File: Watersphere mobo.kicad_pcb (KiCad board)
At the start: 2 copper layers, 74.9 x 81.3 mm, 80 parts, among them IC1 BQ25303JRTER, J2 Conn_01x01_Pin, J3 Conn_01x01_Pin, J4 691213710002, J5 Pressure Sensor I/O, U1 ADS1115IDGSR, U12 LP55231SQE_NOPB, U2 ADS1115IDGSR, U3 TPS63001DRCR, U4 BNO055, U5 ADP1109AN-12, U6 ADP1109AN-12, U7 ADA3708, U8 MIC2876-5.0YMT-TR

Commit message: Routing begin
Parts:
- removed D2, D3: 1N5818, Diode_THT:D_DO-41_SOD81_P10.16mm_Horizontal
- added C16: 1 uF, Capacitor_SMD:C_0603_1608Metric_Pad1.08x0.95mm_HandSolder, F.Cu at (68.1, 78.1)
- added C30: 22uF, Capacitor_SMD:C_0603_1608Metric_Pad1.08x0.95mm_HandSolder, F.Cu at (51.4, 43.4)
- added C31: 22uF, Capacitor_SMD:C_0603_1608Metric_Pad1.08x0.95mm_HandSolder, F.Cu at (53.9, 43.4)
- added C32: 22uF, Capacitor_SMD:C_0603_1608Metric_Pad1.08x0.95mm_HandSolder, F.Cu at (56.4, 43.4)
- added C33: 2.2uF, Capacitor_SMD:C_0603_1608Metric_Pad1.08x0.95mm_HandSolder, F.Cu at (59.8, 39.9)
- added C34: 4.7nf, Capacitor_SMD:C_0603_1608Metric_Pad1.08x0.95mm_HandSolder, F.Cu at (53.2, 38.2)
- added C35: optional, Capacitor_SMD:C_0603_1608Metric_Pad1.08x0.95mm_HandSolder, F.Cu at (54.0, 40.8)
- added C36: optional, Capacitor_SMD:C_0603_1608Metric_Pad1.08x0.95mm_HandSolder, F.Cu at (50.2, 52.3)
- added C37: 4.7nf, Capacitor_SMD:C_0603_1608Metric_Pad1.08x0.95mm_HandSolder, F.Cu at (51.9, 52.3)
- added C38: 22uF, Capacitor_SMD:C_0603_1608Metric_Pad1.08x0.95mm_HandSolder, F.Cu at (61.7, 51.4)
- added C39: 22uF, Capacitor_SMD:C_0603_1608Metric_Pad1.08x0.95mm_HandSolder, F.Cu at (53.5, 56.0)
- added C40: 100nF, Capacitor_SMD:C_0603_1608Metric_Pad1.08x0.95mm_HandSolder, F.Cu at (60.8, 58.3)
- added C41: 22uF, Capacitor_SMD:C_0603_1608Metric_Pad1.08x0.95mm_HandSolder, F.Cu at (51.2, 56.0)
- added C42: 22uF, Capacitor_SMD:C_0603_1608Metric_Pad1.08x0.95mm_HandSolder, F.Cu at (55.7, 56.0)
- added C43: 2.2uF, Capacitor_SMD:C_0603_1608Metric_Pad1.08x0.95mm_HandSolder, F.Cu at (59.1, 52.8)
- added J6: Pressure Sensor I/O, Connector_PinHeader_2.54mm:PinHeader_1x03_P2.54mm_Vertical, F.Cu at (69.7, 96.9)
- added J7: Pressure Sensor I/O, Connector_PinHeader_2.54mm:PinHeader_1x03_P2.54mm_Vertical, F.Cu at (58.3, 96.9)
- added R19: 301k, Resistor_SMD:R_0603_1608Metric_Pad0.98x0.95mm_HandSolder, F.Cu at (61.5, 41.5)
- added R20: 681k, Resistor_SMD:R_0603_1608Metric_Pad0.98x0.95mm_HandSolder, F.Cu at (58.2, 39.9)
- added R21: 107k, Resistor_SMD:R_0603_1608Metric_Pad0.98x0.95mm_HandSolder, F.Cu at (56.5, 39.9)
- added R22: 127k, Resistor_SMD:R_0603_1608Metric_Pad0.98x0.95mm_HandSolder, F.Cu at (57.5, 46.5)
- added R23: 17.4k, Resistor_SMD:R_0603_1608Metric_Pad0.98x0.95mm_HandSolder, F.Cu at (54.9, 38.2)
- added R24: 17.4k, Resistor_SMD:R_0603_1608Metric_Pad0.98x0.95mm_HandSolder, F.Cu at (53.7, 52.3)
- added R25: 681k, Resistor_SMD:R_0603_1608Metric_Pad0.98x0.95mm_HandSolder, F.Cu at (56.4, 53.1)
- added R26: 127k, Resistor_SMD:R_0603_1608Metric_Pad0.98x0.95mm_HandSolder, F.Cu at (56.9, 59.3)
- added R27: 107k, Resistor_SMD:R_0603_1608Metric_Pad0.98x0.95mm_HandSolder, F.Cu at (56.4, 51.3)
- added R28: 301k, Resistor_SMD:R_0603_1608Metric_Pad0.98x0.95mm_HandSolder, F.Cu at (60.8, 54.7)
- C14: value 10 uF -> 22uF
- C15: value 10 uF -> 100nF
- J5: footprint Connector_PinSocket_2.54mm:PinSocket_1x03_P2.54mm_Horizontal -> Connector_PinHeader_2.54mm:PinHeader_1x03_P2.54mm_Vertical
- L3, L4: value L -> 1.8uH; footprint 12v Power Ind:46473C -> 9V_Power_IND:IND_7030-WE-LHMI_WRE-L
- Pump1Controller1, Pump2Controller1, ReactionWheel1Controller1, ReactionWheel2Controller1: footprint Motor_Controller:SOT6_DRV8212_TEX -> DRV8212:SOT6_DRV8212_TEX-L
- U5, U6: value ADP1109AN-12 -> TPS61089RNRR; footprint ADP1109:N_8_ADI -> TPS61089:IC_TPS61089RNRR
- moved R18 112.7 mm to (59.2, 84.7), turned to 90 degrees
- moved C11 110.4 mm to (51.6, 72.3)
- moved C27 107.3 mm to (56.3, 83.7), turned to 180 degrees
- moved C28 107.2 mm to (56.3, 85.6), turned to 180 degrees
- moved R9 102.1 mm to (63.8, 68.3), turned to -90 degrees
- moved R8 102.0 mm to (63.8, 64.8), turned to -90 degrees
- moved R15 100.9 mm to (69.6, 68.3), turned to -90 degrees
- moved C29 100.6 mm to (61.7, 81.5), turned to -90 degrees
- moved R11 99.7 mm to (65.8, 68.3), turned to -90 degrees
- moved R10 99.7 mm to (65.8, 64.8), turned to -90 degrees
- moved R6 99.3 mm to (61.7, 64.8), turned to -90 degrees
- moved R7 99.3 mm to (61.7, 68.3), turned to -90 degrees
- moved R13 97.7 mm to (67.7, 64.8), turned to 90 degrees
- moved R12 97.7 mm to (67.7, 68.3), turned to 90 degrees
- moved R14 95.9 mm to (69.6, 64.8), turned to -90 degrees
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- renumbered RW1 to ReactionWheel1, RW2 to ReactionWheel2
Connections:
- net 12v(1)_meas renamed 9v(1)_meas
- net 12v(2)_meas renamed 9v(2)_meas
- 100uF1 pad 1: 12v(1) -> 9v(1)
- 100uF2 pad 1: 12v(2) -> 9v(2)
- 100uF3 pad 1: 12v(1) -> 9v(1)
- 100uF4 pad 1: 12v(2) -> 9v(2)
- C12 pad 1: 12v(1) -> 9v(1)
- C13 pad 1: 12v(2) -> 9v(2)
- C14 pad 1: 12v(1) -> BAT+
- C15 pad 1: 12v(2) -> Net-(U5-BOOT)
- C15 pad 2: GND -> Net-(U5-SW)
- C21 pad 1: 12v(1) -> 9v(1)
- C22 pad 1: 12v(2) -> 9v(2)
- D1 pad 1: (no net) -> Net-(D1-PadA)
- D1 pad 2: (no net) -> Net-(IC1-STAT)
- L3 pad 1: Net-(D2-A) -> BAT+
- L3 pad 2: BAT+ -> Net-(U5-SW)
- L4 pad 1: Net-(D3-A) -> BAT+
- L4 pad 2: BAT+ -> Net-(U6-SW)
- Pump1Controller1 pad 5: 12v(1) -> 9v(1)
- Pump2Controller1 pad 5: 12v(2) -> 9v(2)
- R12 pad 1: 12v(1)_Shutdown -> 9v(1)
- R14 pad 1: 12v(2)_Shutdown -> 9v(2)
- R18 pad 2: BNO_BOOTN -> Net-(U4-NBOOT_LOAD_PIN)
- ReactionWheel1Controller1 pad 5: 12v(1) -> 9v(1)
- ReactionWheel2Controller1 pad 5: 12v(2) -> 9v(2)
- U4 pad 11: unconnected-(U4-NRESET-Pad11) -> BNO_BOOTN
- U4 pad 17: unconnected-(U4-COM3-Pad17) -> GND
- U4 pad 4: BNO_BOOTN -> Net-(U4-NBOOT_LOAD_PIN)
- U4 pad 5: unconnected-(U4-PS1-Pad5) -> GND
- U4 pad 6: unconnected-(U4-PS0-Pad6) -> GND
- U5 pad 1: BAT+ -> Net-(U5-FSW)
- U5 pad 2: unconnected-(U5-NC-Pad2) -> Net-(U5-VCC)
- U5 pad 3: Net-(D2-A) -> Net-(U5-FB)
- U5 pad 4: GND -> Net-(U5-COMP)
- U5 pad 5: unconnected-(U5-NC-Pad5) -> GND
- U5 pad 6: unconnected-(U5-NC-Pad6) -> 9v(1)
- U5 pad 7: 12v(1)_Shutdown -> 9v(1)_Shutdown
- U5 pad 8: 12v(1) -> Net-(U5-ILIM)
- U6 pad 1: BAT+ -> Net-(U6-FSW)
- U6 pad 2: unconnected-(U6-NC-Pad2) -> Net-(U6-VCC)
- U6 pad 3: Net-(D3-A) -> Net-(U6-FB)
- U6 pad 4: GND -> Net-(U6-COMP)
- U6 pad 5: unconnected-(U6-NC-Pad5) -> GND
- U6 pad 6: unconnected-(U6-NC-Pad6) -> 9v(2)
- U6 pad 7: 12v(2)_Shutdown -> 9v(2)_Shutdown
- U6 pad 8: 12v(2) -> Net-(U6-ILIM)
- U7 pad 4: +5v -> Rasp_Vsupply
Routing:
- net BAT+: track 0.00 -> 112.2 mm
- net REGN: track 0.00 -> 12.9 mm, vias 0 -> 2
- net Net-(U3-EN): track 0.00 -> 11.8 mm
- net VIN: track 0.00 -> 11.3 mm
- net +3.3V: track 0.00 -> 7.66 mm
- net Net-(IC1-ICHG): track 0.00 -> 7.33 mm
- net Net-(U3-L1): track 0.00 -> 5.42 mm
- net Net-(U3-L2): track 0.00 -> 5.23 mm
- net Net-(IC1-TS): track 0.00 -> 5.19 mm
- net Net-(IC1-STAT): track 0.00 -> 4.77 mm
- net Net-(IC1-SW_1): track 0.00 -> 4.40 mm
- net Net-(IC1-BTST): track 0.00 -> 4.24 mm
- net Net-(J1-VCC): track 0.00 -> 2.80 mm
- net Net-(D1-PadA): track 0.00 -> 2.27 mm
- net Net-(IC1-PMID): track 0.00 -> 2.21 mm
- added copper zone on F.Cu, net GND
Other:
- outline, holes or cut-outs redrawn
- copper layers 2 -> 4
- board text added: "P2"
- board text added: "RW1"
- board text added: "RW2"
- board text removed: "D3"

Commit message: Deesign Rules
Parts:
- U5: value TPS61089RNRR -> |
- moved R16 25.1 mm to (51.0, 77.3), turned to -90 degrees
- moved R17 25.0 mm to (48.5, 77.4), turned to -90 degrees
- moved C23 4.74 mm to (42.6, 22.4), turned to 0 degrees
- moved U12 4.54 mm to (37.4, 20.5)
- moved R13 3.58 mm to (67.7, 68.3), turned to -90 degrees
- moved R12 3.53 mm to (67.7, 64.8), turned to -90 degrees
- moved C24 2.58 mm to (48.8, 25.9), turned to 0 degrees
- moved C25 2.24 mm to (43.8, 20.0)
- moved C26 1.99 mm to (48.8, 27.5)
- moved C11 1.24 mm to (52.6, 71.6)
- moved C27 1.22 mm to (56.4, 84.9)
- moved C28 1.22 mm to (56.3, 86.8)
- moved R18 1.22 mm to (59.2, 85.9)
- moved C20 0.98 mm to (81.9, 66.5)
- moved C29 0.55 mm to (61.2, 81.5)
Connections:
- D1 pad 1: Net-(D1-PadA) -> (no net)
- D1 pad 2: Net-(IC1-STAT) -> (no net)
- U12 pad 25: (no net) -> GND
- U2 pad 6: unconnected-(U2-AIN2-Pad6) -> Misc. Sensor 1
- U2 pad 7: unconnected-(U2-AIN3-Pad7) -> Misc. Sensor 2
- U3 pad 12: (no net) -> GND
- U3 pad 13: (no net) -> GND
- U3 pad 14: (no net) -> GND
- U3 pad 15: (no net) -> GND
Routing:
- net +5v: track 0.00 -> 170.6 mm, vias 0 -> 6
- net I2C_Bus1_SDA: track 0.00 -> 141.1 mm, vias 0 -> 4
- net I2C_Bus1_SCL: track 0.00 -> 140.5 mm, vias 0 -> 5
- net 9v(2): track 0.00 -> 109.6 mm, vias 0 -> 4
- net +3.3V: track 7.66 -> 116.7 mm, vias 0 -> 4
- net 9v(1): track 0.00 -> 105.1 mm, vias 0 -> 5
- net PWM_4: track 0.00 -> 63.8 mm, vias 0 -> 2
- net PWM_3: track 0.00 -> 58.2 mm, vias 0 -> 2
- net GND: track 0.00 -> 53.2 mm, vias 0 -> 29
- net BNO_BOOTN: track 0.00 -> 51.6 mm, vias 0 -> 1
- net PWM_2: track 0.00 -> 47.9 mm, vias 0 -> 2
- net BNO_Data_Ready: track 0.00 -> 47.4 mm, vias 0 -> 1
- net PWM_1: track 0.00 -> 44.2 mm, vias 0 -> 2
- net Misc. Sensor 2: track 0.00 -> 43.9 mm, vias 0 -> 1
- net BAT+: track 112.2 -> 155.8 mm
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- added copper zone on B.Cu, net GND
- added copper zone on In1.Cu, net GND
- added copper zone on In2.Cu, net GND

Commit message: gps started
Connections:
- D1 pad 1: (no net) -> Net-(D1-PadA)
- D1 pad 2: (no net) -> Net-(IC1-STAT)
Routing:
- net GND: track 53.2 -> 103.5 mm, vias 29 -> 34
- net +5v: track 170.6 -> 151.6 mm
- net +3.3V: track 116.7 -> 128.9 mm, vias 4 -> 5
- net I2C_Bus1_SDA: track 141.1 -> 147.1 mm

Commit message: Tedi Check dis over pls.
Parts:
- added C17: 10 uF, Capacitor_SMD:C_0603_1608Metric_Pad1.08x0.95mm_HandSolder, F.Cu at (66.7, 82.2)
- added C18: 100nF, Capacitor_SMD:C_0603_1608Metric_Pad1.08x0.95mm_HandSolder, F.Cu at (66.7, 79.7)
- added J8: JST_02, Connector_JST:JST_EH_B2B-EH-A_1x02_P2.50mm_Vertical, F.Cu at (34.3, 96.3)
- added Q1: AO3400A, N-Channel:SOT95P280X125-3N, F.Cu at (29.0, 93.3)
- added R29: 10k, Resistor_SMD:R_0603_1608Metric_Pad0.98x0.95mm_HandSolder, F.Cu at (24.0, 93.6)
- added U10: 734120114, UFL:73412-0114_MOL, F.Cu at (88.2, 80.4)
- added U9: TESEO-LIV3R, Teseo Liv3r:ARRAY_LIV3R_STM, F.Cu at (74.0, 77.2)
- U5: value | -> TPS61089RNRR
- moved C16 3.45 mm to (64.6, 77.7)
- moved MC1 3.45 mm to (63.5, 74.4)
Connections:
- U7 pad 29: unconnected-(U7-GPIO5-Pad29) -> Solenoid_Driver
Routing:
- net Solenoid_Driver: track 0.00 -> 64.9 mm
- net I2C_Bus1_SDA: track 147.1 -> 160.3 mm, vias 4 -> 6
- net I2C_Bus1_SCL: track 140.5 -> 148.9 mm, vias 5 -> 7
- net Net-(U10-SIGNAL): track 0.00 -> 8.01 mm
- net GND: track 103.5 -> 97.7 mm, vias 34 -> 42
- net +3.3V: track 128.9 -> 134.4 mm
- net Net-(J8-Pad1): track 0.00 -> 5.11 mm
- net +5v: track 151.6 -> 152.7 mm
- net 9v(1): vias 5 -> 4
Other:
- outline, holes or cut-outs redrawn

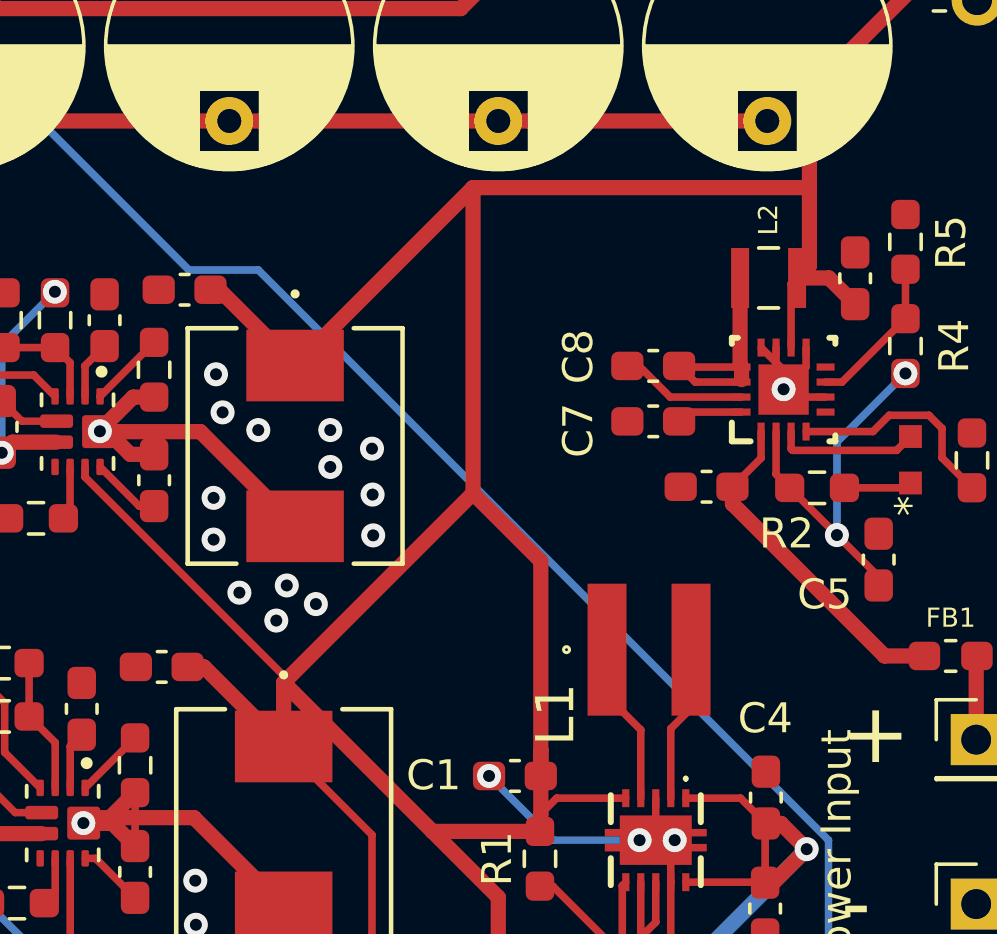
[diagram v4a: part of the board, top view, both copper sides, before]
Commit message: Updated a couple traces
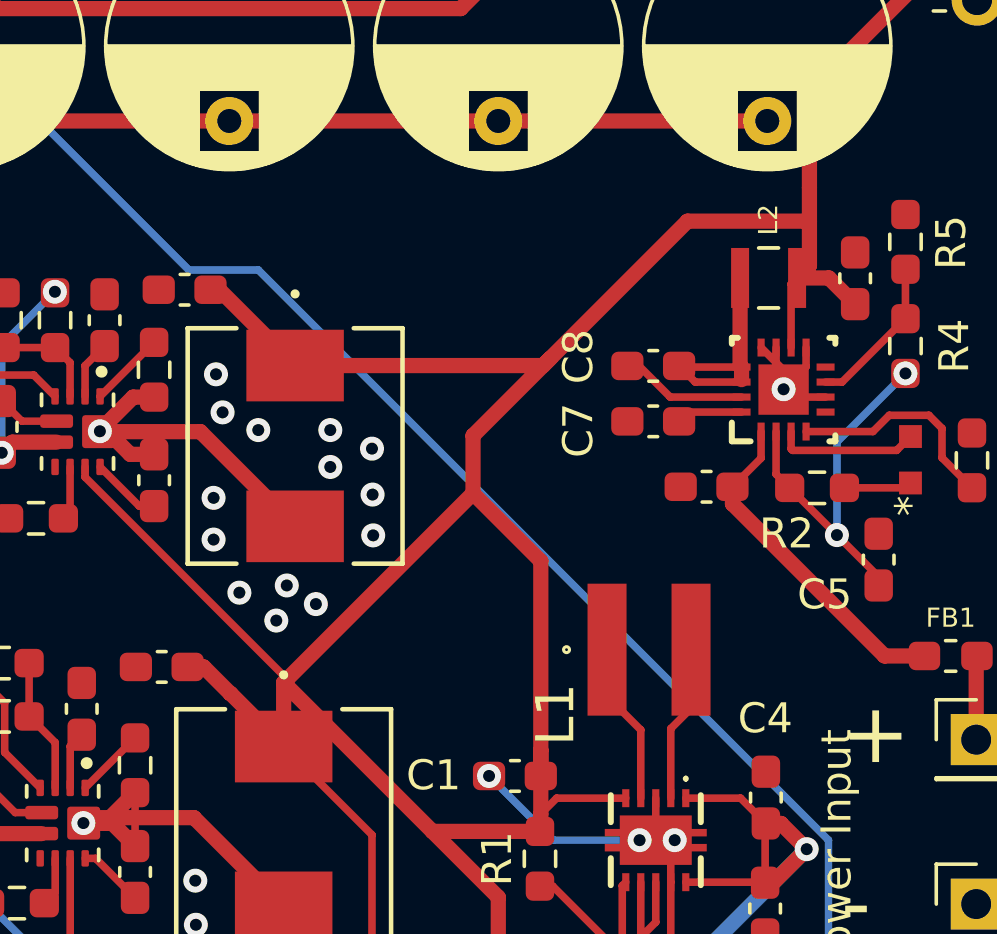
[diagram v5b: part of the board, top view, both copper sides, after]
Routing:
- net BAT+: track 155.8 -> 150.7 mm
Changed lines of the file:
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@@
   (segment (start 74.3575 56.3372) (end 74.3575 56.89) (width 0.508) (layer "F.Cu") (net 1))
   (segment (start 61.722 63.8735) (end 58.67 60.8215) (width 0.254) (layer "F.Cu") (net 1))
+  (segment (start 64.008 52.324) (end 63.119 51.435) (width 0.508) (layer "F.Cu") (net 1))
   (segment (start 58.67 60.8215) (end 58.67 57.817) (width 0.254) (layer "F.Cu") (net 1))
+  (segment (start 83.312 35.4584) (end 83.312 36.576) (width 0.508) (layer "F.Cu") (net 1))
   (segment (start 74.9703 68.663) (end 75.5678 69.2605) (width 0.254) (layer "F.Cu") (net 1))
+  (segment (start 72.0979 45.64741) (end 72.0979 43.7261) (width 0.508) (layer "F.Cu") (net 1))
   (segment (start 74.2703 67.5805) (end 74.9703 67.5805) (width 0.508) (layer "F.Cu") (net 1))
   (segment (start 61.722 63.8735) (end 63.4455 62.15) (width 0.254) (layer "F.Cu") (net 1))
-  (segment (start 83.312 35.4584) (end 83.312 38.057997) (width 0.508) (layer "F.Cu") (net 1))
-  (segment (start 72.0979 35.4584) (end 66.167 41.3893) (width 0.508) (layer "F.Cu") (net 1))
   (segment (start 82.7 38.669997) (end 82.9 38.469997) (width 0.254) (layer "F.Cu") (net 1))
   (segment (start 63.4455 62.15) (end 67.16 62.15) (width 0.254) (layer "F.Cu") (net 1))
@@
   (segment (start 78.24 68.25) (end 79.107 69.117) (width 0.254) (layer "F.Cu") (net 1))
   (segment (start 65.786 51.728324) (end 65.786 54.0893) (width 0.254) (layer "F.Cu") (net 1))
+  (segment (start 63.119 51.435) (end 62.5845 51.435) (width 0.508) (layer "F.Cu") (net 1))
   (segment (start 72.0979 45.64741) (end 74.3575 47.90701) (width 0.508) (layer "F.Cu") (net 1))
   (segment (start 76.5783 68.25) (end 78.24 68.25) (width 0.254) (layer "F.Cu") (net 1))
@@
   (segment (start 77.19 55.81) (end 74.8847 55.81) (width 0.254) (layer "F.Cu") (net 1))
   (segment (start 65.786 51.95931) (end 70.74419 56.9175) (width 0.508) (layer "F.Cu") (net 1))
+  (segment (start 83.312 36.576) (end 83.312 38.057997) (width 0.508) (layer "F.Cu") (net 1))
+  (segment (start 65.786 54.0893) (end 64.0207 52.324) (width 0.508) (layer "F.Cu") (net 1))
   (segment (start 88.9 26.67) (end 83.312 32.258) (width 0.508) (layer "F.Cu") (net 1))
   (segment (start 68.73 57.0333) (end 65.786 54.0893) (width 0.254) (layer "F.Cu") (net 1))
@@
   (segment (start 59.166 45.108324) (end 65.786 51.728324) (width 0.254) (layer "F.Cu") (net 1))
   (segment (start 79.861134 69.117) (end 80.29 68.688134) (width 0.254) (layer "F.Cu") (net 1))
-  (segment (start 65.786 54.0893) (end 63.1317 51.435) (width 0.508) (layer "F.Cu") (net 1))
-  (segment (start 72.0979 35.4584) (end 72.0979 45.64741) (width 0.508) (layer "F.Cu") (net 1))
   (segment (start 70.74419 56.9175) (end 74.33 56.9175) (width 0.508) (layer "F.Cu") (net 1))
   (segment (start 83.312 32.258) (end 83.312 35.4584) (width 0.508) (layer "F.Cu") (net 1))
   (segment (start 80.29 68.688134) (end 80.29 67.474101) (width 0.254) (layer "F.Cu") (net 1))
   (segment (start 68.73 60.58) (end 68.73 57.0333) (width 0.254) (layer "F.Cu") (net 1))
+  (segment (start 79.248 36.576) (end 83.312 36.576) (width 0.508) (layer "F.Cu") (net 1))
+  (segment (start 72.0979 43.7261) (end 79.248 36.576) (width 0.508) (layer "F.Cu") (net 1))
   (segment (start 63.6397 38.862) (end 63.3465 38.862) (width 0.508) (layer "F.Cu") (net 1))
   (segment (start 72.0979 45.64741) (end 65.786 51.95931) (width 0.508) (layer "F.Cu") (net 1))
@@
   (segment (start 74.3575 54.2036) (end 74.3575 56.3372) (width 0.508) (layer "F.Cu") (net 1))
   (segment (start 80.29 67.474101) (end 79.867899 67.052) (width 0.254) (layer "F.Cu") (net 1))
-  (segment (start 63.1317 51.435) (end 62.5845 51.435) (width 0.508) (layer "F.Cu") (net 1))
+  (segment (start 74.4347 41.3893) (end 66.167 41.3893) (width 0.508) (layer "F.Cu") (net 1))
   (segment (start 82.9 38.469997) (end 83.962497 38.469997) (width 0.508) (layer "F.Cu") (net 1))
   (segment (start 82.7 40.79) (end 82.7 38.669997) (width 0.254) (layer "F.Cu") (net 1))
   (segment (start 83.312 38.057997) (end 82.9 38.469997) (width 0.508) (layer "F.Cu") (net 1))
-  (segment (start 83.312 35.4584) (end 72.0979 35.4584) (width 0.508) (layer "F.Cu") (net 1))
+  (segment (start 74.676 41.148) (end 74.4347 41.3893) (width 0.508) (layer "F.Cu") (net 1))
   (segment (start 74.3575 56.89) (end 74.33 56.9175) (width 0.508) (layer "F.Cu") (net 1))
   (segment (start 77.4787 67.052) (end 75.4988 67.052) (width 0.254) (layer "F.Cu") (net 1))
   (segment (start 75.5678 69.2605) (end 76.5783 68.25) (width 0.254) (layer "F.Cu") (net 1))
+  (segment (start 64.0207 52.324) (end 64.008 52.324) (width 0.508) (layer "F.Cu") (net 1))
   (segment (start 72.94 59.11331) (end 72.94 66.2502) (width 0.508) (layer "F.Cu") (net 1))
   (segment (start 77.4787 66.051999) (end 75.341799 66.051999) (width 0.254) (layer "F.Cu") (net 2))
@@
     (connect_pads (clearance 0.5))
     (min_thickness 0.25) (filled_areas_thickness no)
-    (fill yes (thermal_gap 0.5) (thermal_bridge_width 0.5))
+    (fill (thermal_gap 0.5) (thermal_bridge_width 0.5))
     (polygon
       (pts
